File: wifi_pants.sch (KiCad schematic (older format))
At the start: 23 parts, among them P1 CONN_02X20, P2 POWER / UART, P3 JST PH POWER IN, U1 ESP-12E, U2 TPS61252

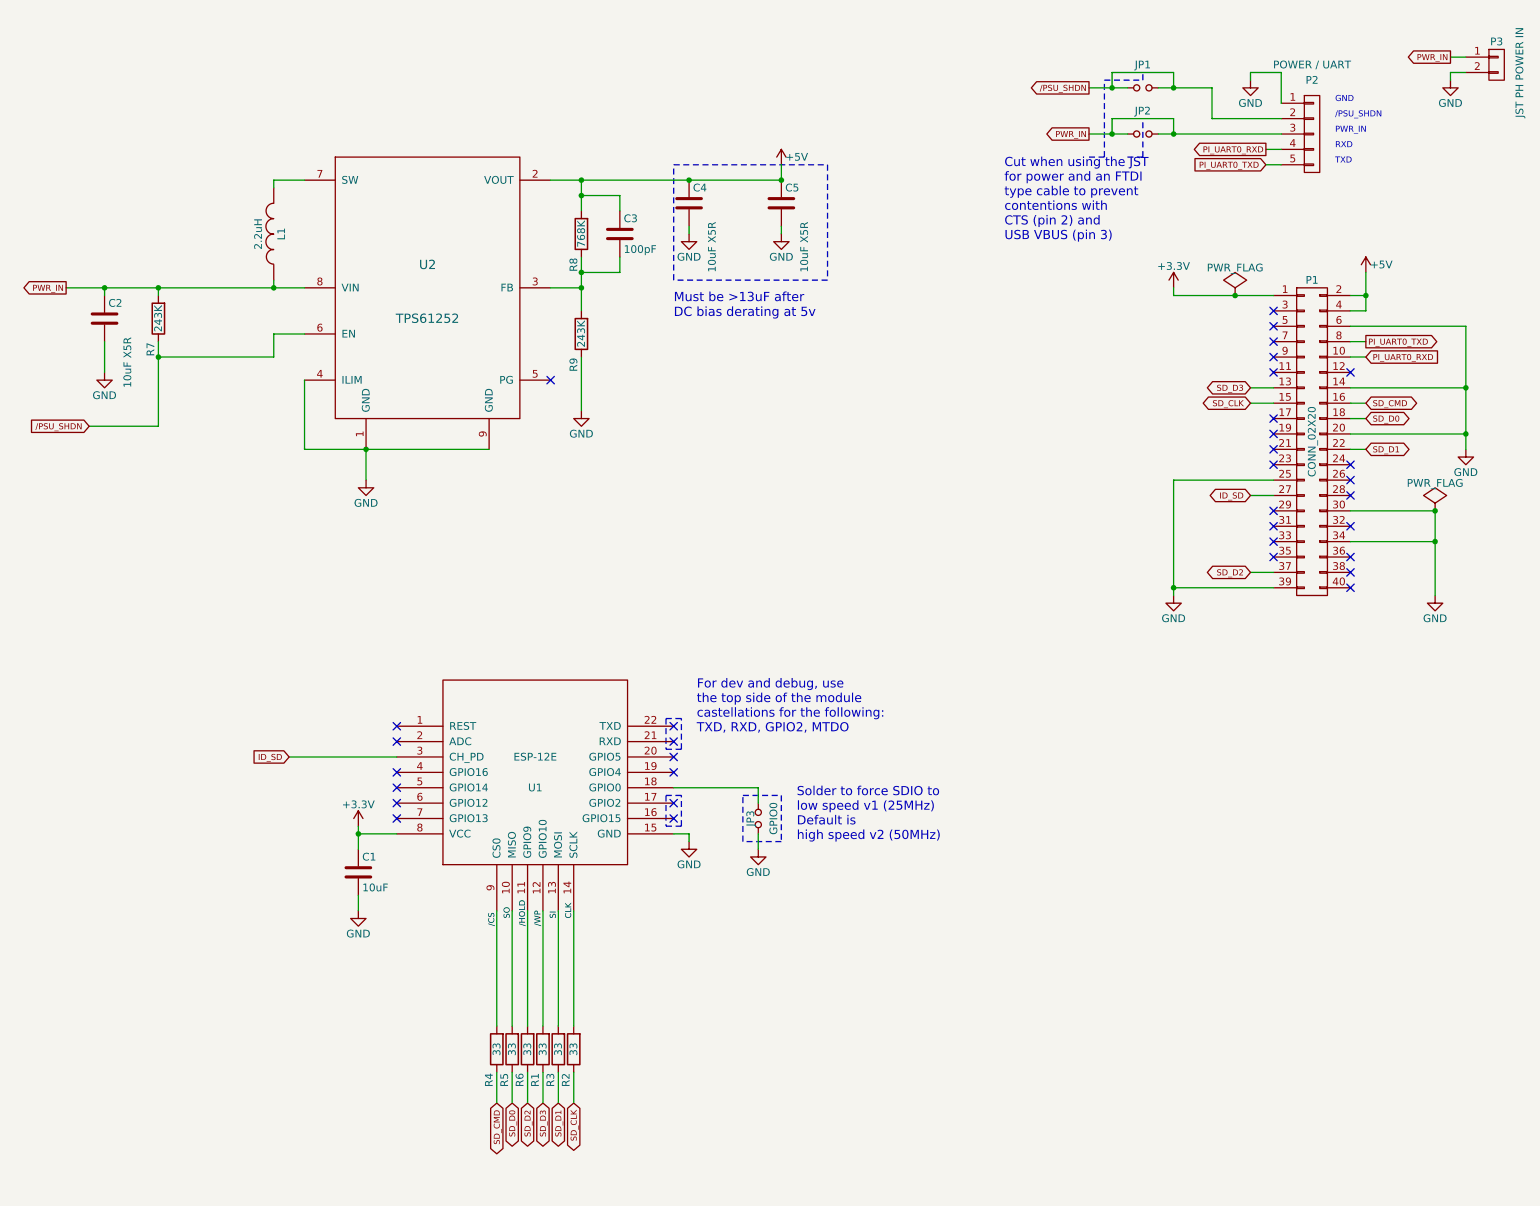
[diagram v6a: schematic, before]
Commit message: Changed to a different switcher
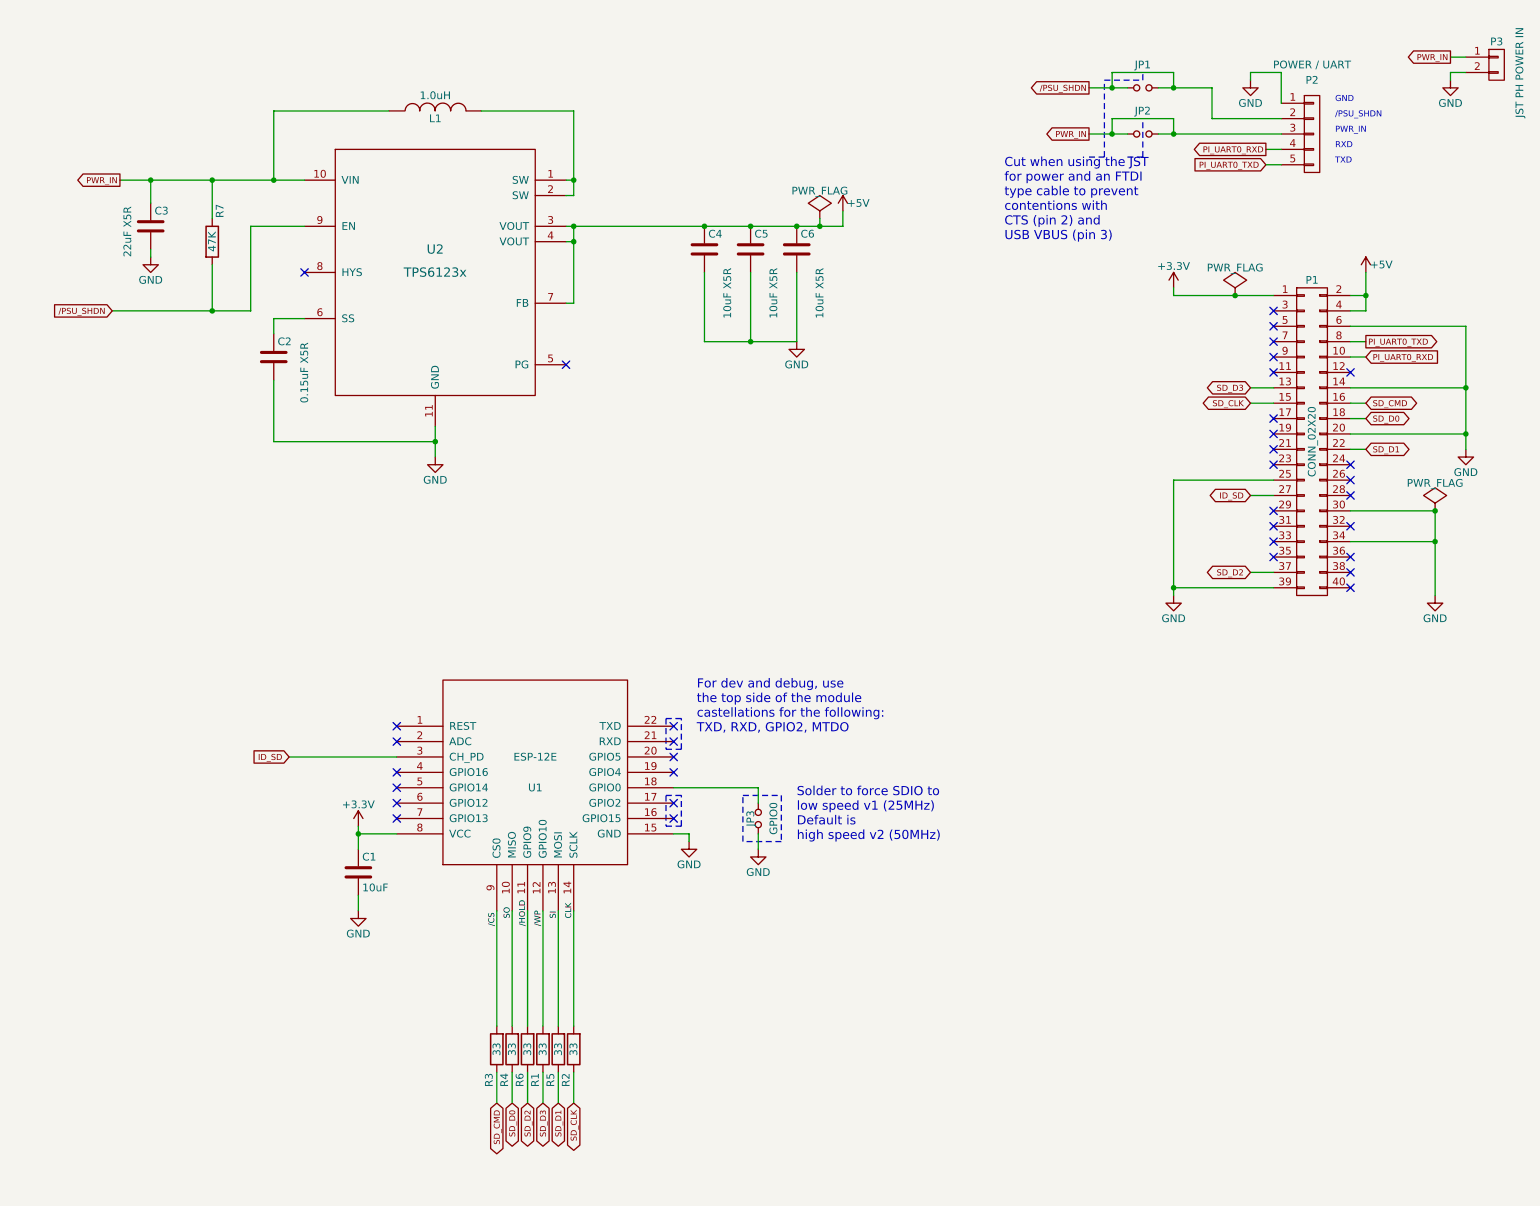
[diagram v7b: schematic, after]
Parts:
- removed C4: 10uF X5R, mcous:1206(3216m)-CHIP-CAP, symbol C
- removed R8: 768K, mcous:0603(1608m)-CHIP-RESISTOR, symbol R
- removed R9: 243K, mcous:0603(1608m)-CHIP-RESISTOR, symbol R
- removed U2: TPS61252, wifi_pants:WSON-8-1EP_2x2mm_Pitch0.5mm, symbol TPS61252
- added C2: 0.15uF X5R, mcous:0603(1608m)-CHIP-CAP, symbol C
- added C6: 10uF X5R, mcous:0805(2012m)-CHIP-CAP, symbol C
- added U2: TPS6123x, wifi_pants:VSON-10, symbol TPS6123x
- C3: value 100pF -> 22uF X5R; Digikey Link http://www.digikey.com/product-detail/en/GRM1885C1H101JA01D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 -> http://www.digikey.com/product-detail/en/LMK212BJ226MG-T/58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; Digikey PN 490-1427-1-ND -> 587-1958-1-ND; MFG Name Murata Electronics North America -> Taiyo Yuden; MFG Part Num GRM1885C1H101JA01D -> LMK212BJ226MG-T
- C4: renamed from C2; footprint mcous:1206(3216m)-CHIP-CAP -> mcous:0805(2012m)-CHIP-CAP; Digikey Link http://www.digikey.com/product-detail/en/GRM219R60J106KE19D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 -> http://www.digikey.com/product-detail/en/LMK212BJ106KG-T/58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; Digikey PN 587-1342-1-ND -> 587-1300-1-ND; MFG Part Num LMK316BJ106KL-T -> LMK212BJ106KG-T
- C5: footprint mcous:1206(3216m)-CHIP-CAP -> mcous:0805(2012m)-CHIP-CAP; Digikey Link http://www.digikey.com/product-detail/en/GRM219R60J106KE19D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 -> http://www.digikey.com/product-detail/en/LMK212BJ106KG-T/58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; Digikey PN 587-1342-1-ND -> 587-1300-1-ND; MFG Part Num LMK316BJ106KL-T -> LMK212BJ106KG-T
- L1: value 2.2uH -> 1.0uH; footprint wifi_pants:NR6028 -> wifi_pants:SRU1028-1R; Digikey Link http://www.digikey.com/product-detail/en/NR6028T2R2N/587-20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 -> http://www.digikey.com/product-detail/en/SRU1028-1R0Y/SRU10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; Digikey PN 587-2098-1-ND -> SRU1028-1R0YCT-ND; MFG Name Taiyo Yuden -> Bourns; MFG Part Num NR6028T2R2N -> SRU1028-1R0Y
- R7: value 243K -> 47K; Digikey Link http://www.digikey.com/product-detail/en/ERJ-3EKF2433V/P243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 -> http://www.digikey.com/product-detail/en/ERJ-3GEYJ223V/P22K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; Digikey PN P243KHCT-ND -> P22KGCT-ND; MFG Part Num ERJ-3EKF2433V -> ERJ-3GEYJ223V
- renumbered R4 to R3, R5 to R4, R3 to R5
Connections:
- net +5V: now also C4.1, C6.1, U2.3 (VOUT), U2.4 (VOUT), U2.7 (FB); no longer C3.1
- net /PSU_SHDN: now also R7.2, U2.9 (EN); no longer R7.1
- net GND: now also C3.2, C2.2, C6.2, U2.11 (GND)
- net PWR_IN: now also C3.1, R7.1, U2.10 (VIN); no longer C4.1, R7.2
- net at L1.2: now also U2.1 (SW), U2.2 (SW)
- new net: C2.1, U2.6 (SS)
- no-connect marks 34 -> 35
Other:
- note removed: "Must be >13uF after\nDC bias derating at 5v"
- moved on the sheet: C4, L1, R7

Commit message: Clean up PSU layout and silk
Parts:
- C1: value 10uF -> 10uF X5R; Digikey Link http://www.digikey.com/product-detail/en/GRM219R60J106KE19D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 -> http://www.digikey.com/product-detail/en/LMK212BJ106KG-T/58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; Digikey PN 490-3340-1-ND -> 587-1300-1-ND; MFG Name Murata Electronics North America -> Taiyo Yuden; MFG Part Num GRM219R60J106KE19D -> LMK212BJ106KG-T
- JP1: value Jumper_NO_Small -> /PSU_SHDN ISOL
- JP2: value Jumper_NO_Small -> PWR_IN ISOL
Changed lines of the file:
@@
-	1    0    0    -1
-$EndComp
-$Comp
-L C C1
-U 1 1 56945510
-P 2750 6100
-F 0 "C1" H 2775 6200 50  0000 L CNN
-F 1 "10uF" H 2775 6000 50  0000 L CNN
-F 2 "mcous:0805(2012m)-CHIP-CAP" H 2788 5950 50  0001 C CNN
-F 3 "" H 2750 6100 50  0000 C CNN
-F 4 "Murata Electronics North America" H 2750 6100 60  0001 C CNN "MFG Name"
-F 5 "GRM219R60J106KE19D" H 2750 6100 60  0001 C CNN "MFG Part Num"
-F 6 "490-3340-1-ND" H 2750 6100 60  0001 C CNN "Digikey PN"
-F 7 "http://www.digikey.com/product-detail/en/GRM219R60J106KE19D/490-3340-1-ND/702881" H 2750 6100 60  0001 C CNN "Digikey Link"
-F 8 "NA" H 2750 6100 60  0001 C CNN "2nd Distrib PN"
-F 9 "NA" H 2750 6100 60  0001 C CNN "2nd Distrib Link"
-	1    2750 6100
 	1    0    0    -1
 $EndComp
@@
 U 1 1 56BC717F
 P 7850 1300
-F 0 "JP2" H 7850 1450 50  0000 C CNN
-F 1 "Jumper_NO_Small" H 7860 1240 50  0001 C CNN
+F 0 "JP2" H 7850 1450 50  0001 C CNN
+F 1 "PWR_IN ISOL" H 7860 1240 50  0000 C CNN
 F 2 "wifi_pants:GS2" H 7850 1300 50  0001 C CNN
 F 3 "" H 7850 1300 50  0000 C CNN
@@
 U 1 1 56BC71CA
 P 7850 1000
-F 0 "JP1" H 7850 1150 50  0000 C CNN
-F 1 "Jumper_NO_Small" H 7860 940 50  0001 C CNN
+F 0 "JP1" H 7850 1150 50  0001 C CNN
+F 1 "/PSU_SHDN ISOL" H 7860 940 50  0000 C CNN
 F 2 "wifi_pants:GS2" H 7850 1000 50  0001 C CNN
 F 3 "" H 7850 1000 50  0000 C CNN
@@
 	5750 1850 5750 1900
 Connection ~ 5750 1900
+$Comp
+L C C1
+U 1 1 56BF8AF0
+P 2750 6100
+F 0 "C1" H 2775 6200 50  0000 L CNN
+F 1 "10uF X5R" V 2900 5650 50  0000 L CNN
+F 2 "mcous:0805(2012m)-CHIP-CAP" H 2788 5950 50  0001 C CNN
+F 3 "http://ds.yuden.co.jp/TYCOMPAS/ut/detail.do?productNo=LMK316BJ106KL-T&fileName=LMK316BJ106KL-T_SS&mode=specSheetDownload" H 2750 6100 50  0001 C CNN
+F 4 "Taiyo Yuden" H 2750 6100 60  0001 C CNN "MFG Name"
+F 5 "LMK212BJ106KG-T" H 2750 6100 60  0001 C CNN "MFG Part Num"
+F 6 "587-1300-1-ND" H 2750 6100 60  0001 C CNN "Digikey PN"
+F 7 "http://www.digikey.com/product-detail/en/LMK212BJ106KG-T/587-1300-1-ND/931077" H 2750 6100 60  0001 C CNN "Digikey Link"
+F 8 "NA" H 2750 6100 60  0001 C CNN "2nd Distrib PN"
+F 9 "NA" H 2750 6100 60  0001 C CNN "2nd Distrib Link"
+	1    2750 6100
+	1    0    0    -1
+$EndComp
 $EndSCHEMATC
